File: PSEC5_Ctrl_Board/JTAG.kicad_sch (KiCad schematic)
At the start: 2 parts, among them J6 878311420, U1 PUSB3FR4Z

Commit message: Large Updates, Touching up before further aproval
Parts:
- renumbered J6 to J?, U1 to U?
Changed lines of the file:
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@@
 		(dnp no)
 		(fields_autoplaced yes)
-		(property "Reference" "U1"
+		(property "Reference" "U?"
 			(at 57.15 82.5499 90)
 			(effects
@@
 		)
 		(instances
-			(project ""
-				(path "/165f2ae6-d522-4adf-a6c4-bb137b209d33/fbf72b83-3438-48d6-962d-3a9c35dd6213"
-					(reference "U1")
+			(project "PSEC5_Ctrl_Board"
+				(path "/165f2ae6-d522-4adf-a6c4-bb137b209d33/fbf72b83-3438-48d6-962d-3a9c35dd6213"
+					(reference "U?")
+					(unit 1)
+				)
+				(path "/165f2ae6-d522-4adf-a6c4-bb137b209d33/0e271294-afb4-40f4-a456-ad11d287e722/3cc94eec-6db4-45df-a125-390e4a553895"
+					(reference "U18")
+					(unit 1)
+				)
+				(path "/165f2ae6-d522-4adf-a6c4-bb137b209d33/1f6d7a03-cfad-4370-8d2b-49ab19e248d8/277fb02f-a6ab-4b05-94e6-c516155fbdc1"
+					(reference "U3")
 					(unit 1)
 				)
@@
 		(dnp no)
 		(fields_autoplaced yes)
-		(property "Reference" "#PWR04"
+		(property "Reference" "#PWR?"
 			(at 62.23 26.67 0)
 			(effects
@@
 		)
 		(instances
-			(project ""
-				(path "/165f2ae6-d522-4adf-a6c4-bb137b209d33/fbf72b83-3438-48d6-962d-3a9c35dd6213"
-					(reference "#PWR04")
+			(project "PSEC5_Ctrl_Board"
+				(path "/165f2ae6-d522-4adf-a6c4-bb137b209d33/fbf72b83-3438-48d6-962d-3a9c35dd6213"
+					(reference "#PWR?")
+					(unit 1)
+				)
+				(path "/165f2ae6-d522-4adf-a6c4-bb137b209d33/0e271294-afb4-40f4-a456-ad11d287e722/3cc94eec-6db4-45df-a125-390e4a553895"
+					(reference "#PWR0108")
+					(unit 1)
+				)
+				(path "/165f2ae6-d522-4adf-a6c4-bb137b209d33/1f6d7a03-cfad-4370-8d2b-49ab19e248d8/277fb02f-a6ab-4b05-94e6-c516155fbdc1"
+					(reference "#PWR062")
 					(unit 1)
 				)
@@
 		(dnp no)
 		(fields_autoplaced yes)
-		(property "Reference" "#PWR03"
+		(property "Reference" "#PWR?"
 			(at 45.72 118.11 0)
 			(effects
@@
 		)
 		(instances
-			(project ""
-				(path "/165f2ae6-d522-4adf-a6c4-bb137b209d33/fbf72b83-3438-48d6-962d-3a9c35dd6213"
-					(reference "#PWR03")
+			(project "PSEC5_Ctrl_Board"
+				(path "/165f2ae6-d522-4adf-a6c4-bb137b209d33/fbf72b83-3438-48d6-962d-3a9c35dd6213"
+					(reference "#PWR?")
+					(unit 1)
+				)
+				(path "/165f2ae6-d522-4adf-a6c4-bb137b209d33/0e271294-afb4-40f4-a456-ad11d287e722/3cc94eec-6db4-45df-a125-390e4a553895"
+					(reference "#PWR0106")
+					(unit 1)
+				)
+				(path "/165f2ae6-d522-4adf-a6c4-bb137b209d33/1f6d7a03-cfad-4370-8d2b-49ab19e248d8/277fb02f-a6ab-4b05-94e6-c516155fbdc1"
+					(reference "#PWR060")
 					(unit 1)
 				)
@@
 		(dnp no)
 		(fields_autoplaced yes)
-		(property "Reference" "J6"
+		(property "Reference" "J?"
 			(at 93.98 35.5599 0)
 			(effects
@@
 		)
 		(instances
-			(project ""
-				(path "/165f2ae6-d522-4adf-a6c4-bb137b209d33/fbf72b83-3438-48d6-962d-3a9c35dd6213"
-					(reference "J6")
+			(project "PSEC5_Ctrl_Board"
+				(path "/165f2ae6-d522-4adf-a6c4-bb137b209d33/fbf72b83-3438-48d6-962d-3a9c35dd6213"
+					(reference "J?")
+					(unit 1)
+				)
+				(path "/165f2ae6-d522-4adf-a6c4-bb137b209d33/0e271294-afb4-40f4-a456-ad11d287e722/3cc94eec-6db4-45df-a125-390e4a553895"
+					(reference "J15")
+					(unit 1)
+				)
+				(path "/165f2ae6-d522-4adf-a6c4-bb137b209d33/1f6d7a03-cfad-4370-8d2b-49ab19e248d8/277fb02f-a6ab-4b05-94e6-c516155fbdc1"
+					(reference "J12")
 					(unit 1)
 				)
@@
 		(dnp no)
 		(fields_autoplaced yes)
-		(property "Reference" "#PWR015"
+		(property "Reference" "#PWR?"
 			(at 60.96 73.66 0)
 			(effects
@@
 		)
 		(instances
-			(project ""
-				(path "/165f2ae6-d522-4adf-a6c4-bb137b209d33/fbf72b83-3438-48d6-962d-3a9c35dd6213"
-					(reference "#PWR015")
+			(project "PSEC5_Ctrl_Board"
+				(path "/165f2ae6-d522-4adf-a6c4-bb137b209d33/fbf72b83-3438-48d6-962d-3a9c35dd6213"
+					(reference "#PWR?")
+					(unit 1)
+				)
+				(path "/165f2ae6-d522-4adf-a6c4-bb137b209d33/0e271294-afb4-40f4-a456-ad11d287e722/3cc94eec-6db4-45df-a125-390e4a553895"
+					(reference "#PWR0107")
+					(unit 1)
+				)
+				(path "/165f2ae6-d522-4adf-a6c4-bb137b209d33/1f6d7a03-cfad-4370-8d2b-49ab19e248d8/277fb02f-a6ab-4b05-94e6-c516155fbdc1"
+					(reference "#PWR061")
 					(unit 1)
 				)
@@
 		(dnp no)
 		(fields_autoplaced yes)
-		(property "Reference" "#PWR02"
+		(property "Reference" "#PWR?"
 			(at 73.66 66.04 0)
 			(effects
@@
 		)
 		(instances
-			(project ""
-				(path "/165f2ae6-d522-4adf-a6c4-bb137b209d33/fbf72b83-3438-48d6-962d-3a9c35dd6213"
-					(reference "#PWR02")
-					(unit 1)
-				)
+			(project "PSEC5_Ctrl_Board"
+				(path "/165f2ae6-d522-4adf-a6c4-bb137b209d33/fbf72b83-3438-48d6-962d-3a9c35dd6213"
+					(reference "#PWR?")
+					(unit 1)
+				)
+				(path "/165f2ae6-d522-4adf-a6c4-bb137b209d33/0e271294-afb4-40f4-a456-ad11d287e722/3cc94eec-6db4-45df-a125-390e4a553895"
+					(reference "#PWR0109")
+					(unit 1)
+				)
+				(path "/165f2ae6-d522-4adf-a6c4-bb137b209d33/1f6d7a03-cfad-4370-8d2b-49ab19e248d8/277fb02f-a6ab-4b05-94e6-c516155fbdc1"
+					(reference "#PWR063")
+					(unit 1)
+				)

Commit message: Schematic is "done" ;( (999+ ERC errors)
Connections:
- no-connect marks 2 -> 3
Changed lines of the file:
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@@
+	)
+	(no_connect
+		(at 29.21 48.26)
 	)
 	(no_connect
@@
 		(pts
 			(xy 29.21 33.02) (xy 48.26 33.02)
+		)
+		(stroke
+			(width 0)
+			(type default)
+		)
+	)
+	(wire
+		(pts
+			(xy 25.4 48.26) (xy 29.21 48.26)
 		)
 		(stroke
@@
 	(hierarchical_label "RST"
 		(shape bidirectional)
-		(at 29.21 48.26 180)
+		(at 25.4 48.26 180)
 		(fields_autoplaced yes)
 		(effects

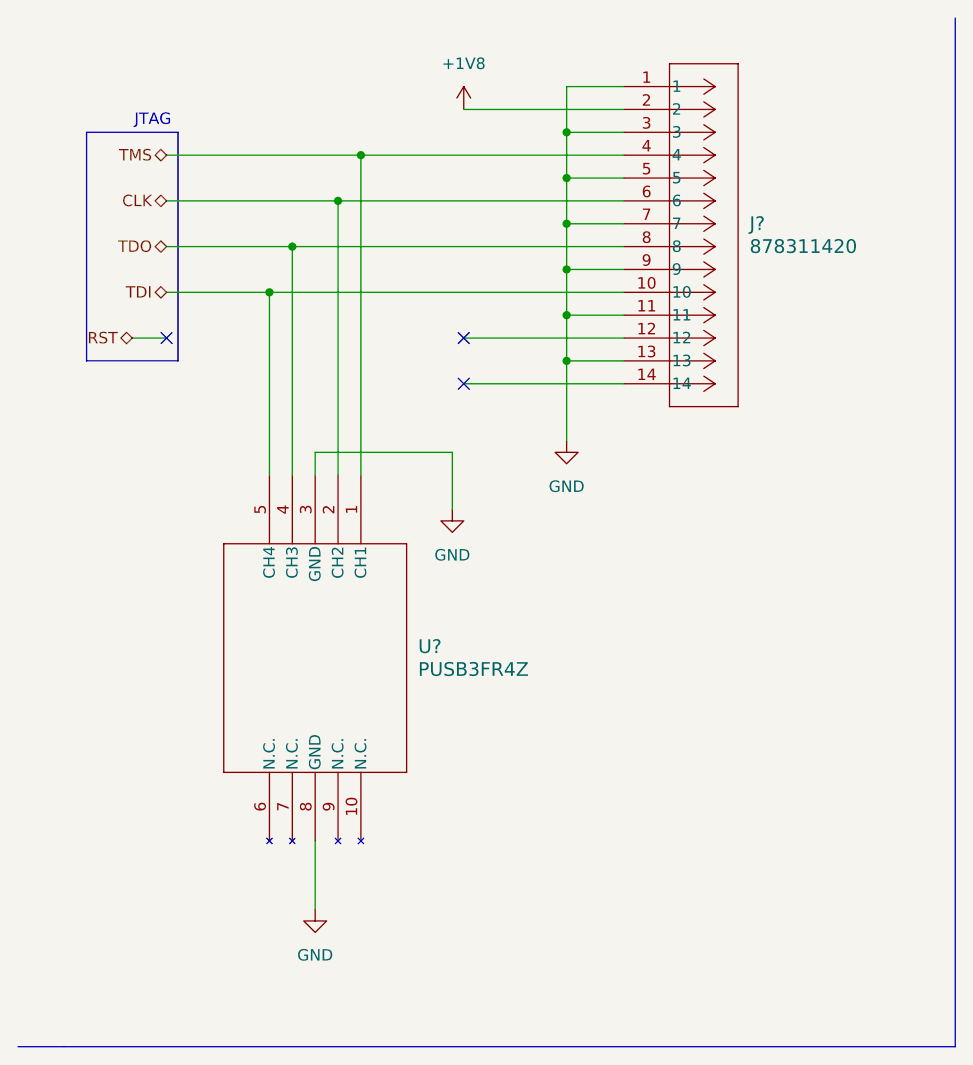
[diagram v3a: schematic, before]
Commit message: changes to schematic errors
Errors should be closer to 897~
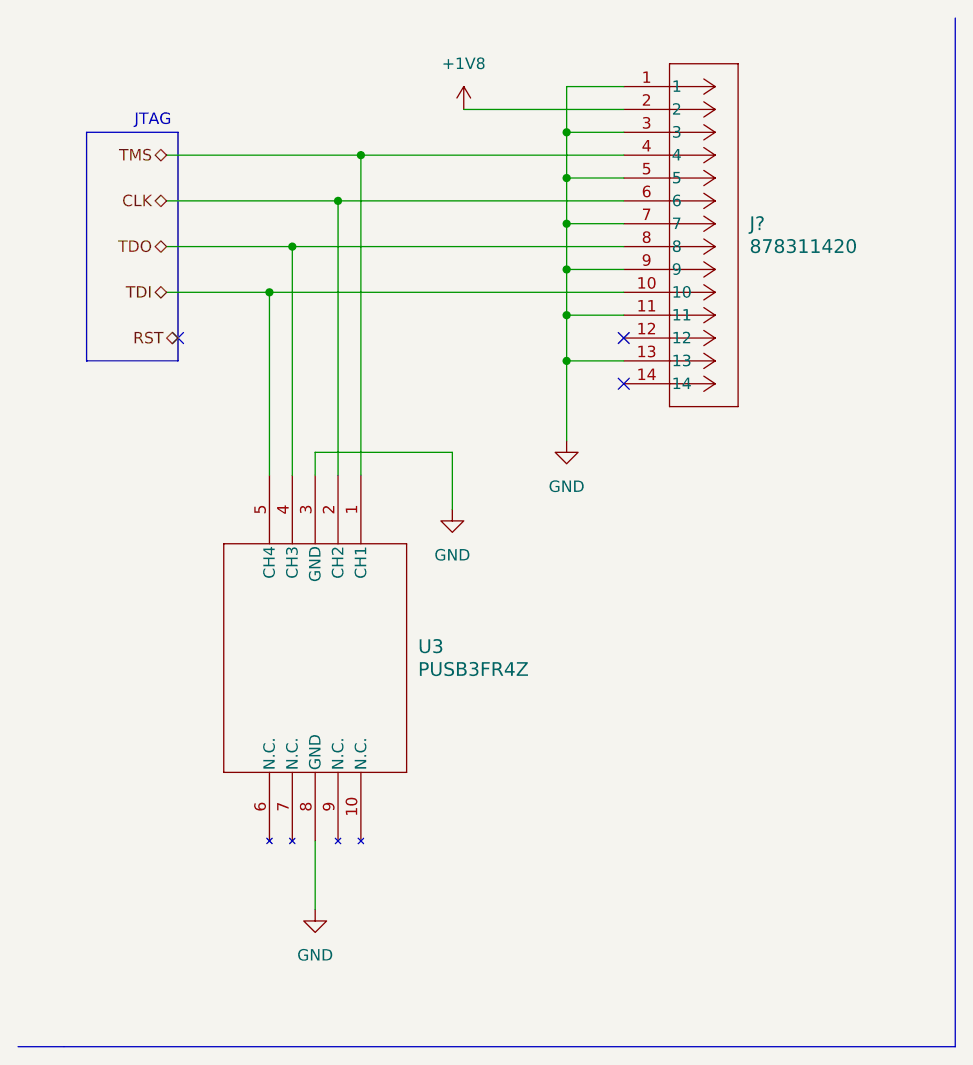
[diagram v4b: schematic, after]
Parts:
- gave numbers to parts that had none: 1
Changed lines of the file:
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@@
 	)
 	(no_connect
-		(at 29.21 48.26)
+		(at 80.01 48.26)
 	)
 	(no_connect
-		(at 62.23 48.26)
+		(at 30.48 48.26)
 	)
 	(no_connect
-		(at 62.23 53.34)
+		(at 80.01 53.34)
 	)
 	(polyline
@@
 	(wire
 		(pts
-			(xy 25.4 48.26) (xy 29.21 48.26)
-		)
-		(stroke
-			(width 0)
-			(type default)
-		)
-	)
-	(wire
-		(pts
 			(xy 40.64 43.18) (xy 80.01 43.18)
 		)
@@
 	(wire
 		(pts
-			(xy 62.23 53.34) (xy 80.01 53.34)
-		)
-		(stroke
-			(width 0)
-			(type default)
-		)
-	)
-	(wire
-		(pts
 			(xy 43.18 38.1) (xy 43.18 63.5)
 		)
@@
 		(pts
 			(xy 50.8 27.94) (xy 50.8 63.5)
-		)
-		(stroke
-			(width 0)
-			(type default)
-		)
-	)
-	(wire
-		(pts
-			(xy 62.23 48.26) (xy 80.01 48.26)
 		)
 		(stroke
@@
 	(hierarchical_label "RST"
 		(shape bidirectional)
-		(at 25.4 48.26 180)
+		(at 30.48 48.26 180)
 		(fields_autoplaced yes)
 		(effects
@@
 		(dnp no)
 		(fields_autoplaced yes)
-		(property "Reference" "U?"
+		(property "Reference" "U3"
 			(at 57.15 82.5499 90)
 			(effects
@@
 			(project "PSEC5_Ctrl_Board"
 				(path "/165f2ae6-d522-4adf-a6c4-bb137b209d33/fbf72b83-3438-48d6-962d-3a9c35dd6213"
-					(reference "U?")
+					(reference "U3")
 					(unit 1)
 				)
@@
 		(dnp no)
 		(fields_autoplaced yes)
-		(property "Reference" "#PWR?"
+		(property "Reference" "#PWR0128"
 			(at 62.23 26.67 0)
 			(effects
@@
 			(project "PSEC5_Ctrl_Board"
 				(path "/165f2ae6-d522-4adf-a6c4-bb137b209d33/fbf72b83-3438-48d6-962d-3a9c35dd6213"
-					(reference "#PWR?")
+					(reference "#PWR0128")
 					(unit 1)
 				)
@@
 		(dnp no)
 		(fields_autoplaced yes)
-		(property "Reference" "#PWR?"
+		(property "Reference" "#PWR0130"
 			(at 45.72 118.11 0)
 			(effects
@@
 			(project "PSEC5_Ctrl_Board"
 				(path "/165f2ae6-d522-4adf-a6c4-bb137b209d33/fbf72b83-3438-48d6-962d-3a9c35dd6213"
-					(reference "#PWR?")
+					(reference "#PWR0130")
 					(unit 1)
 				)
@@
 		(dnp no)
 		(fields_autoplaced yes)
-		(property "Reference" "#PWR?"
+		(property "Reference" "#PWR0131"
 			(at 60.96 73.66 0)
 			(effects
@@
 			(project "PSEC5_Ctrl_Board"
 				(path "/165f2ae6-d522-4adf-a6c4-bb137b209d33/fbf72b83-3438-48d6-962d-3a9c35dd6213"
-					(reference "#PWR?")
+					(reference "#PWR0131")
 					(unit 1)
 				)
@@
 		(dnp no)
 		(fields_autoplaced yes)
-		(property "Reference" "#PWR?"
+		(property "Reference" "#PWR0129"
 			(at 73.66 66.04 0)
 			(effects
@@
 			(project "PSEC5_Ctrl_Board"
 				(path "/165f2ae6-d522-4adf-a6c4-bb137b209d33/fbf72b83-3438-48d6-962d-3a9c35dd6213"
-					(reference "#PWR?")
-					(unit 1)
-				)
+					(reference "#PWR0129")
+					(unit 1)
+				)

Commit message: Deleted some Pages, still lots of errors :(
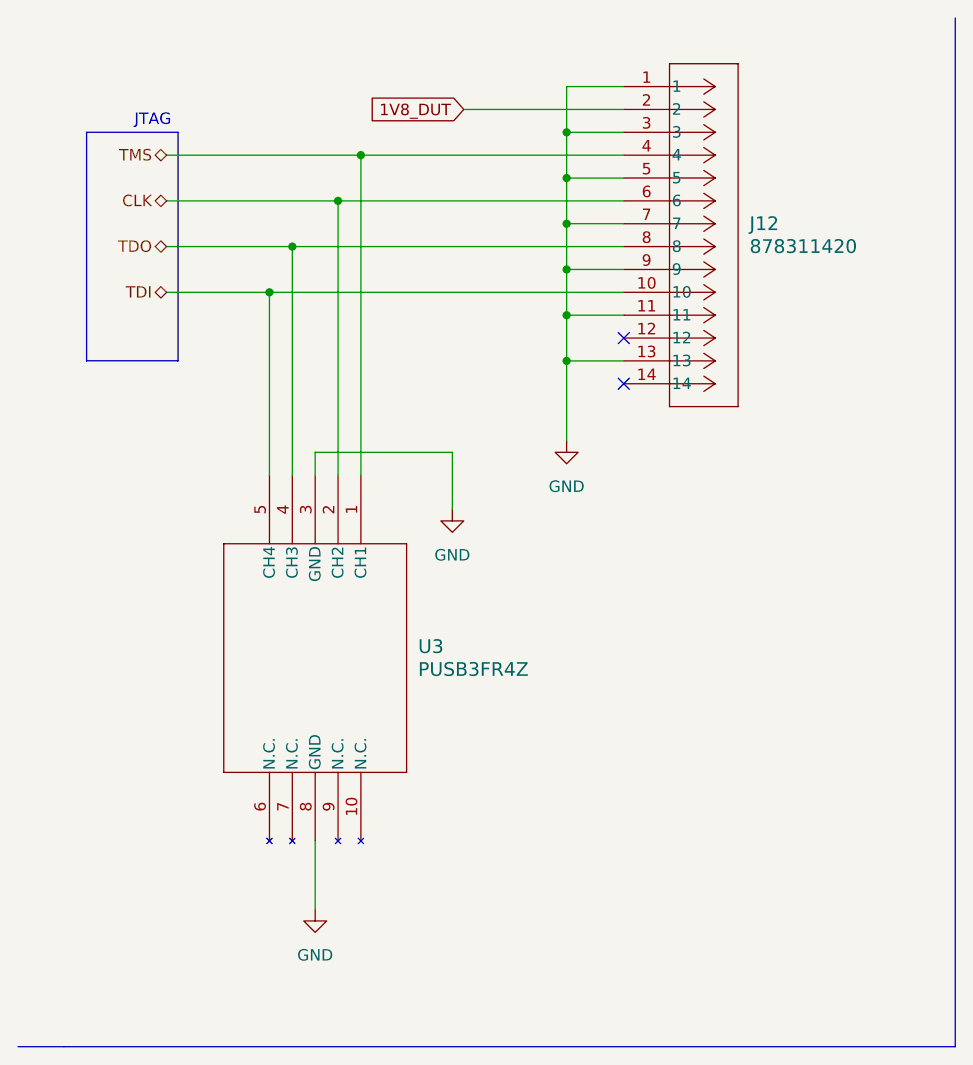
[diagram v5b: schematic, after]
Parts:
- gave numbers to parts that had none: 1
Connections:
- net +1V8 renamed 1V8_DUT
- no-connect marks 3 -> 2
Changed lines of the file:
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@@
-	)
-	(no_connect
-		(at 30.48 48.26)
 	)
 	(no_connect
@@
 		)
 	)
+	(global_label "1V8_DUT"
+		(shape input)
+		(at 62.23 22.86 180)
+		(fields_autoplaced yes)
+		(effects
+			(font
+				(size 1.27 1.27)
+			)
+			(justify right)
+		)
+		(property "Intersheetrefs" "${INTERSHEET_REFS}"
+			(at 51.2015 22.86 0)
+			(effects
+				(font
+					(size 1.27 1.27)
+				)
+				(justify right)
+				(hide yes)
+			)
+		)
+	)
 	(hierarchical_label "TDI"
 		(shape bidirectional)
@@
 		(shape bidirectional)
 		(at 29.21 33.02 180)
-		(fields_autoplaced yes)
-		(effects
-			(font
-				(size 1.27 1.27)
-			)
-			(justify right)
-		)
-	)
-	(hierarchical_label "RST"
-		(shape bidirectional)
-		(at 30.48 48.26 180)
 		(fields_autoplaced yes)
 		(effects
@@
 		(instances
 			(project "PSEC5_Ctrl_Board"
-				(path "/165f2ae6-d522-4adf-a6c4-bb137b209d33/fbf72b83-3438-48d6-962d-3a9c35dd6213"
-					(reference "U3")
-					(unit 1)
-				)
 				(path "/165f2ae6-d522-4adf-a6c4-bb137b209d33/1f6d7a03-cfad-4370-8d2b-49ab19e248d8/277fb02f-a6ab-4b05-94e6-c516155fbdc1"
 					(reference "U3")
-					(unit 1)
-				)
-			)
-		)
-	)
-	(symbol
-		(lib_id "power:+1V8")
-		(at 62.23 22.86 0)
-		(unit 1)
-		(exclude_from_sim no)
-		(in_bom yes)
-		(on_board yes)
-		(dnp no)
-		(fields_autoplaced yes)
-		(property "Reference" "#PWR0128"
-			(at 62.23 26.67 0)
-			(effects
-				(font
-					(size 1.27 1.27)
-				)
-				(hide yes)
-			)
-		)
-		(property "Value" "+1V8"
-			(at 62.23 17.78 0)
-			(effects
-				(font
-					(size 1.27 1.27)
-				)
-			)
-		)
-		(property "Footprint" ""
-			(at 62.23 22.86 0)
-			(effects
-				(font
-					(size 1.27 1.27)
-				)
-				(hide yes)
-			)
-		)
-		(property "Datasheet" ""
-			(at 62.23 22.86 0)
-			(effects
-				(font
-					(size 1.27 1.27)
-				)
-				(hide yes)
-			)
-		)
-		(property "Description" "Power symbol creates a global label with name \"+1V8\""
-			(at 62.23 22.86 0)
-			(effects
-				(font
-					(size 1.27 1.27)
-				)
-				(hide yes)
-			)
-		)
-		(pin "1"
-		)
-		(instances
-			(project "PSEC5_Ctrl_Board"
-				(path "/165f2ae6-d522-4adf-a6c4-bb137b209d33/fbf72b83-3438-48d6-962d-3a9c35dd6213"
-					(reference "#PWR0128")
-					(unit 1)
-				)
-				(path "/165f2ae6-d522-4adf-a6c4-bb137b209d33/1f6d7a03-cfad-4370-8d2b-49ab19e248d8/277fb02f-a6ab-4b05-94e6-c516155fbdc1"
-					(reference "#PWR062")
 					(unit 1)
 				)
@@
 		(dnp no)
 		(fields_autoplaced yes)
-		(property "Reference" "#PWR0130"
+		(property "Reference" "#PWR060"
 			(at 45.72 118.11 0)
 			(effects
@@
 		(instances
 			(project "PSEC5_Ctrl_Board"
-				(path "/165f2ae6-d522-4adf-a6c4-bb137b209d33/fbf72b83-3438-48d6-962d-3a9c35dd6213"
-					(reference "#PWR0130")
-					(unit 1)
-				)
 				(path "/165f2ae6-d522-4adf-a6c4-bb137b209d33/1f6d7a03-cfad-4370-8d2b-49ab19e248d8/277fb02f-a6ab-4b05-94e6-c516155fbdc1"
 					(reference "#PWR060")
@@
 		(dnp no)
 		(fields_autoplaced yes)
-		(property "Reference" "J?"
+		(property "Reference" "J12"
 			(at 93.98 35.5599 0)
 			(effects
@@
 		(instances
 			(project "PSEC5_Ctrl_Board"
-				(path "/165f2ae6-d522-4adf-a6c4-bb137b209d33/fbf72b83-3438-48d6-962d-3a9c35dd6213"
-					(reference "J?")
-					(unit 1)
-				)
 				(path "/165f2ae6-d522-4adf-a6c4-bb137b209d33/1f6d7a03-cfad-4370-8d2b-49ab19e248d8/277fb02f-a6ab-4b05-94e6-c516155fbdc1"
 					(reference "J12")
@@
 		(dnp no)
 		(fields_autoplaced yes)
-		(property "Reference" "#PWR0131"
+		(property "Reference" "#PWR061"
 			(at 60.96 73.66 0)
 			(effects
@@
 		(instances
 			(project "PSEC5_Ctrl_Board"
-				(path "/165f2ae6-d522-4adf-a6c4-bb137b209d33/fbf72b83-3438-48d6-962d-3a9c35dd6213"
-					(reference "#PWR0131")
-					(unit 1)
-				)
 				(path "/165f2ae6-d522-4adf-a6c4-bb137b209d33/1f6d7a03-cfad-4370-8d2b-49ab19e248d8/277fb02f-a6ab-4b05-94e6-c516155fbdc1"
 					(reference "#PWR061")
@@
 		(dnp no)
 		(fields_autoplaced yes)
-		(property "Reference" "#PWR0129"
+		(property "Reference" "#PWR063"
 			(at 73.66 66.04 0)
 			(effects
@@
 		(instances
 			(project "PSEC5_Ctrl_Board"
-				(path "/165f2ae6-d522-4adf-a6c4-bb137b209d33/fbf72b83-3438-48d6-962d-3a9c35dd6213"
-					(reference "#PWR0129")
-					(unit 1)
-				)
 				(path "/165f2ae6-d522-4adf-a6c4-bb137b209d33/1f6d7a03-cfad-4370-8d2b-49ab19e248d8/277fb02f-a6ab-4b05-94e6-c516155fbdc1"
 					(reference "#PWR063")

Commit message: Minor Schematic Changes, ERC still haunts me :(
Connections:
- net 1V8_DUT renamed 1V8_IO
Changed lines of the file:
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@@
 		)
 	)
-	(global_label "1V8_DUT"
+	(global_label "1V8_IO"
 		(shape input)
 		(at 62.23 22.86 180)
@@
 		)
 		(property "Intersheetrefs" "${INTERSHEET_REFS}"
-			(at 51.2015 22.86 0)
+			(at 52.8343 22.86 0)
 			(effects
 				(font

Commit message: Changes
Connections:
- net 1V8_IO renamed 1V8_Banks
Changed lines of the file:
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@@
 		)
 	)
-	(global_label "1V8_IO"
+	(global_label "1V8_Banks"
 		(shape input)
 		(at 62.23 22.86 180)
@@
 		)
 		(property "Intersheetrefs" "${INTERSHEET_REFS}"
-			(at 52.8343 22.86 0)
+			(at 49.1454 22.86 0)
 			(effects
 				(font
